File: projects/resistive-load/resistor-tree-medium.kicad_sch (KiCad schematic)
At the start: 24 parts, among them Q19 PJP45N06A_T0_00001, Q20 PJP45N06A_T0_00001, Q21 PJP45N06A_T0_00001, Q22 PJP45N06A_T0_00001

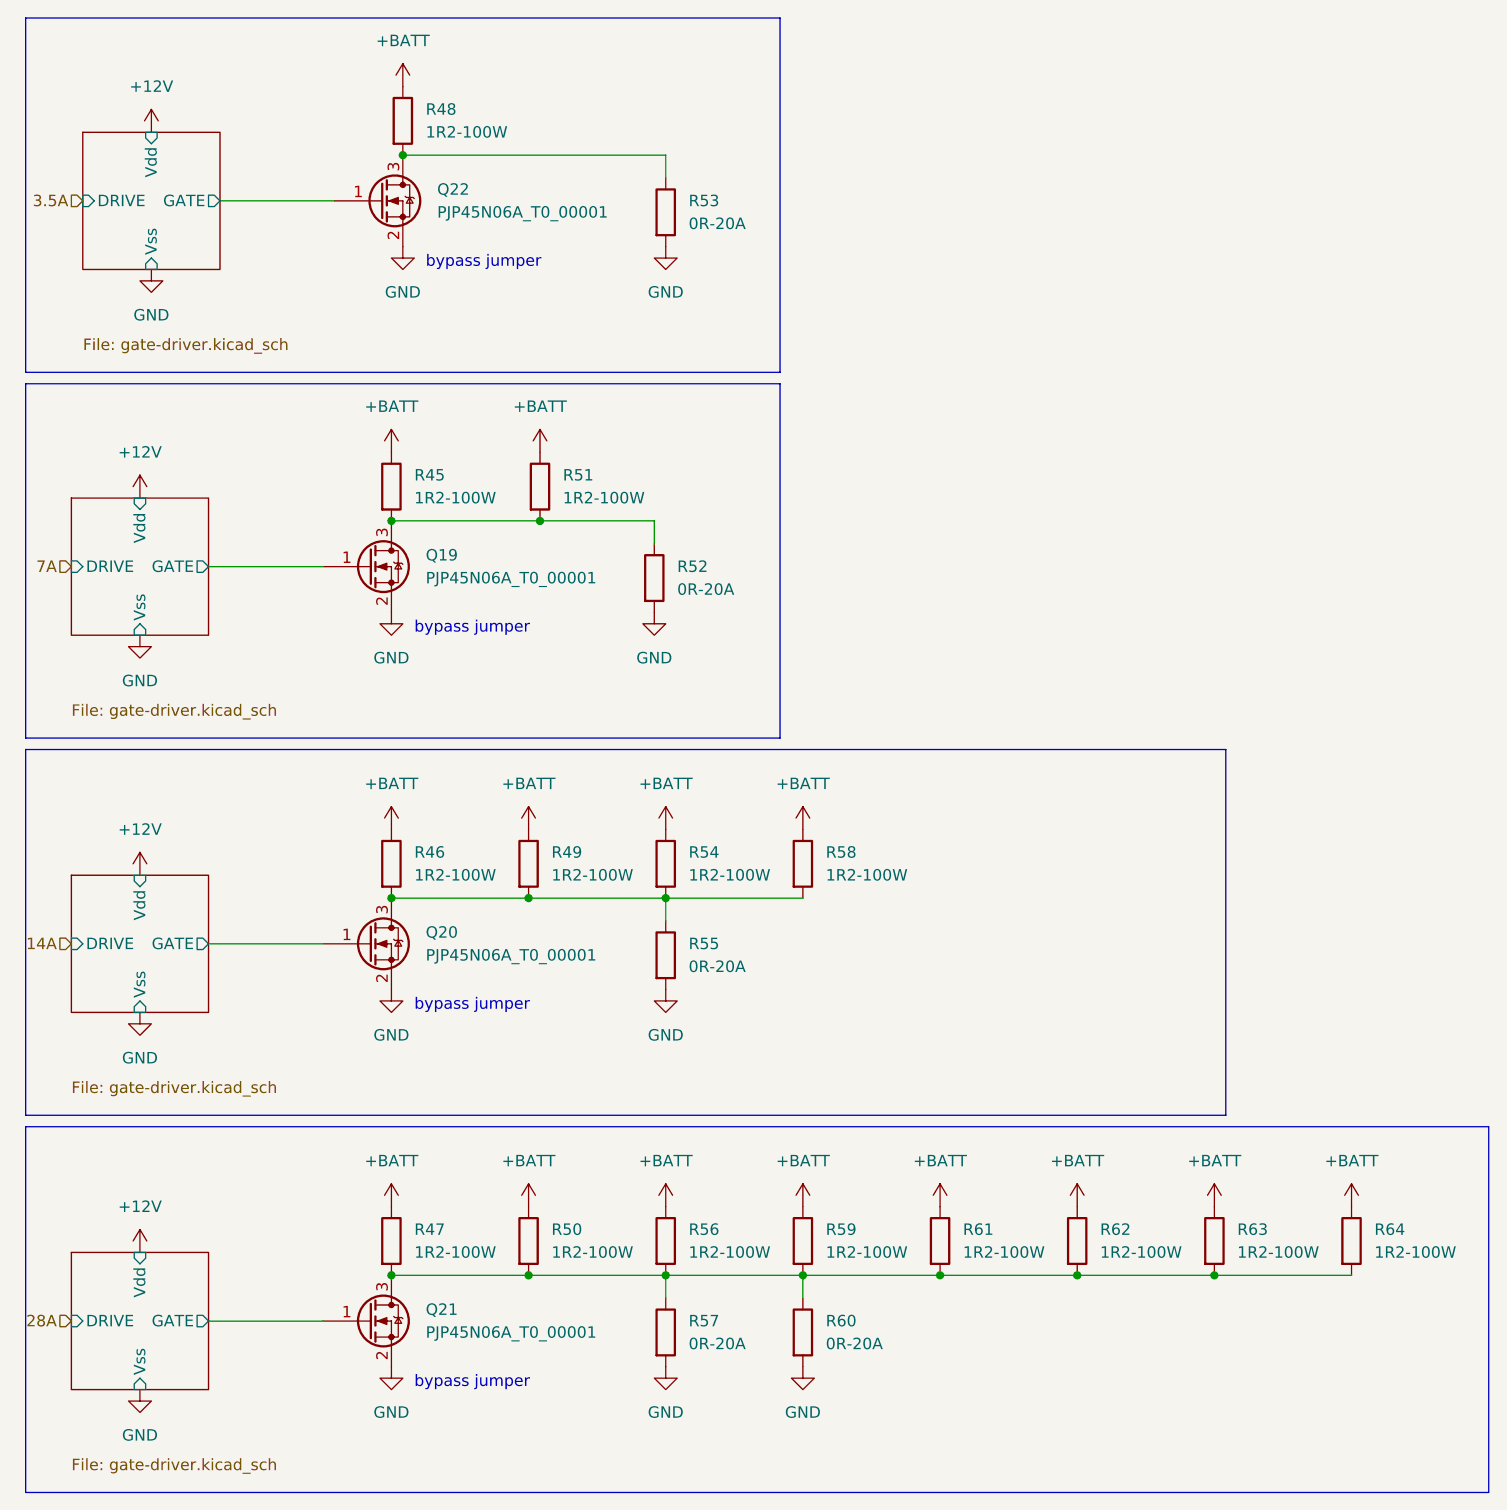
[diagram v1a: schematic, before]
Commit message: fix: update pin assignment for transistors
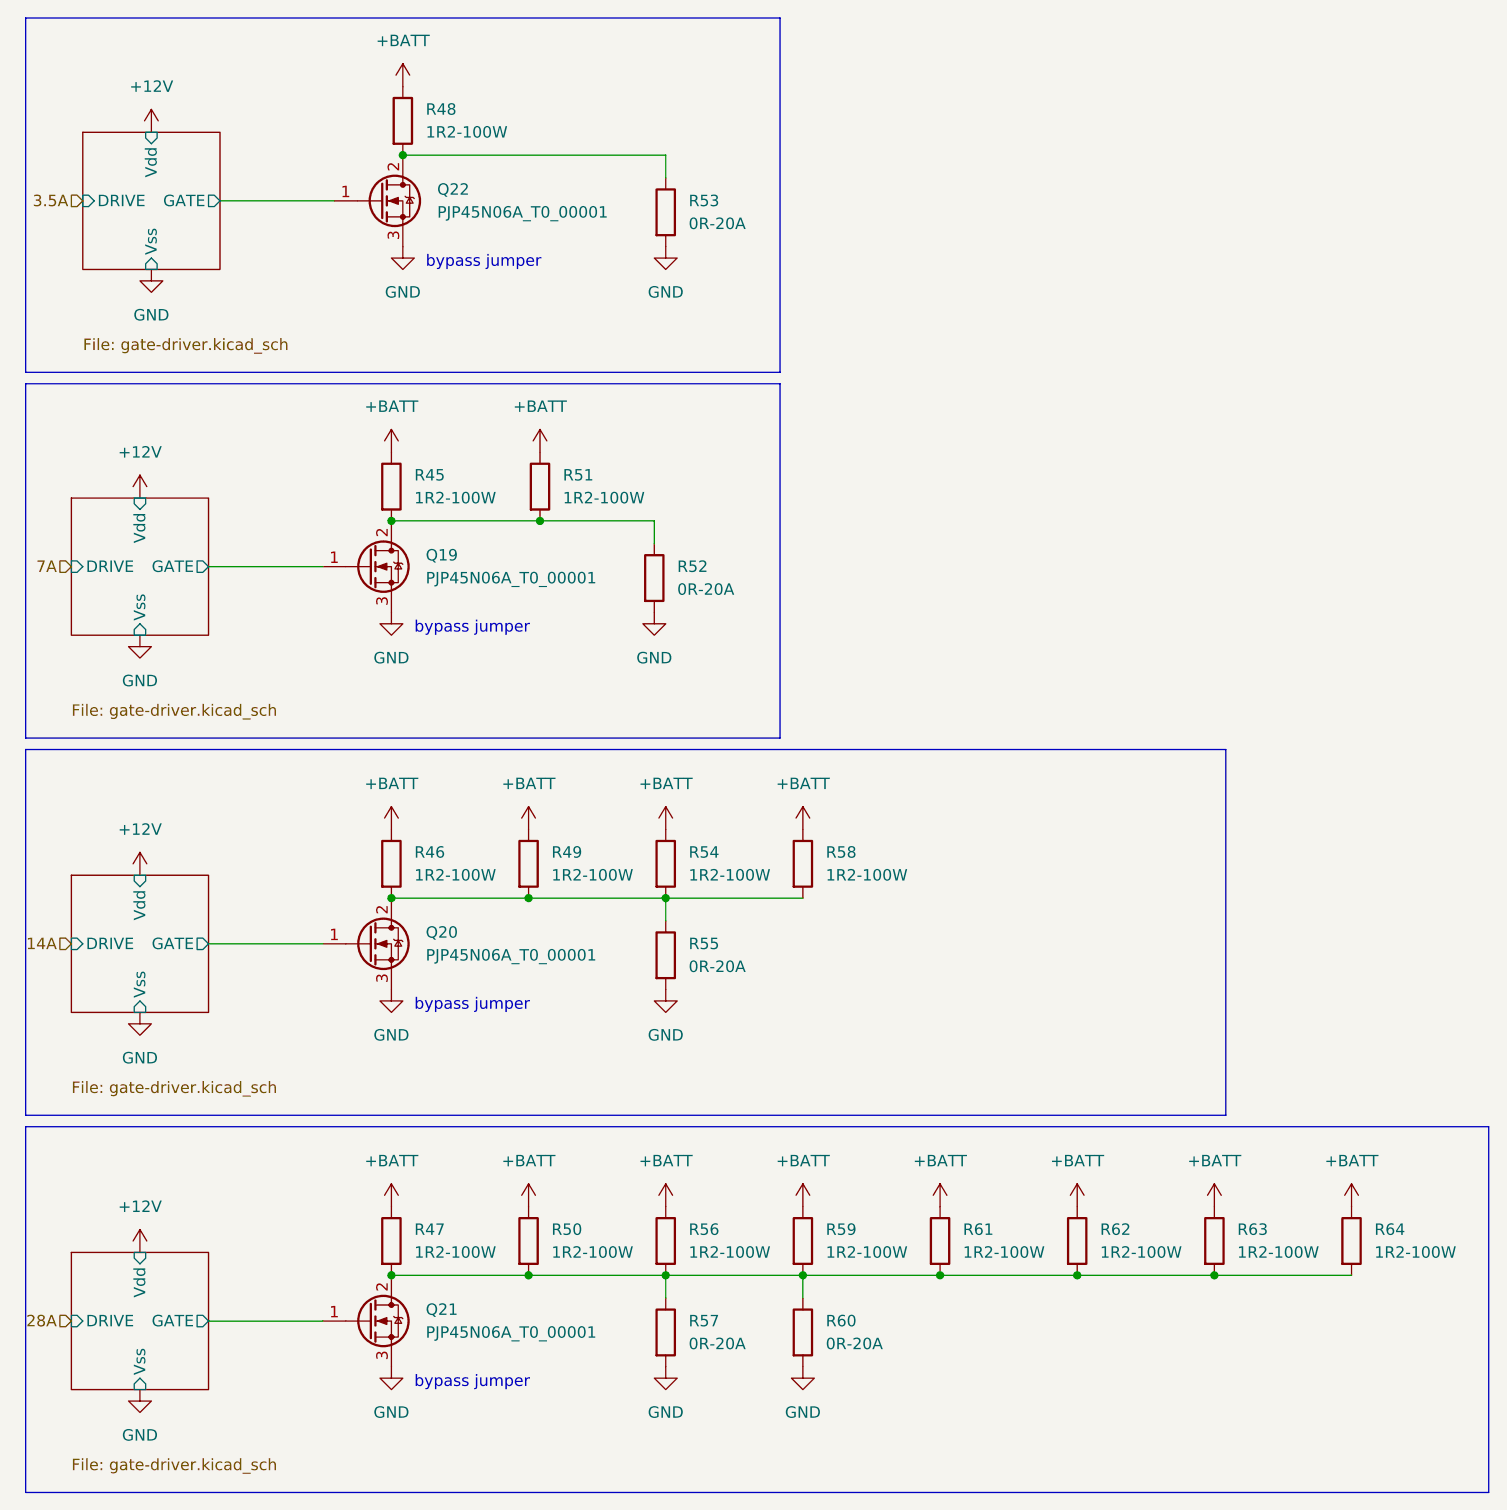
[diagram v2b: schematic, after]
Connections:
- net GND: now also Q19.3 (S), Q20.3 (S), Q21.3 (S), Q22.3 (S); no longer Q19.2 (S), Q20.2 (S), Q21.2 (S), Q22.2 (S)
- net at R47.2, R50.2, R56.2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: now also Q21.2 (D); no longer Q21.3 (D)
- net at R46.2, R49.2, R54.2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: now also Q20.2 (D); no longer Q20.3 (D)
- net at R48.2, R53.1: now also Q22.2 (D); no longer Q22.3 (D)
- net at R45.2, R51.2, R52.1: now also Q19.2 (D); no longer Q19.3 (D)
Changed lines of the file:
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@@
   (symbol (lib_id "power:GND") (at 82.55 80.01 0) (unit 1)
     (in_bom yes) (on_board yes) (fields_autoplaced)
-    (property "Reference" "#PWR0207" (id 0) (at 82.55 86.36 0)
+    (property "Reference" "#PWR?" (id 0) (at 82.55 86.36 0)
       (effects (font (size 1.27 1.27)) hide)
     )
@@
   (symbol (lib_id "power:+BATT") (at 68.58 104.14 0) (unit 1)
     (in_bom yes) (on_board yes) (fields_autoplaced)
-    (property "Reference" "#PWR0218" (id 0) (at 68.58 107.95 0)
+    (property "Reference" "#PWR?" (id 0) (at 68.58 107.95 0)
       (effects (font (size 1.27 1.27)) hide)
     )
@@
   (symbol (lib_id "power:GND") (at 25.4 82.55 0) (unit 1)
     (in_bom yes) (on_board yes) (fields_autoplaced)
-    (property "Reference" "#PWR0199" (id 0) (at 25.4 88.9 0)
+    (property "Reference" "#PWR?" (id 0) (at 25.4 88.9 0)
       (effects (font (size 1.27 1.27)) hide)
     )
@@
   (symbol (lib_id "power:+BATT") (at 53.34 146.05 0) (unit 1)
     (in_bom yes) (on_board yes) (fields_autoplaced)
-    (property "Reference" "#PWR0216" (id 0) (at 53.34 149.86 0)
+    (property "Reference" "#PWR?" (id 0) (at 53.34 149.86 0)
       (effects (font (size 1.27 1.27)) hide)
     )
@@
   (symbol (lib_id "power:+12V") (at 25.4 109.22 0) (unit 1)
     (in_bom yes) (on_board yes) (fields_autoplaced)
-    (property "Reference" "#PWR0214" (id 0) (at 25.4 113.03 0)
+    (property "Reference" "#PWR?" (id 0) (at 25.4 113.03 0)
       (effects (font (size 1.27 1.27)) hide)
     )
@@
   (symbol (lib_id "power:+BATT") (at 54.61 21.59 0) (unit 1)
     (in_bom yes) (on_board yes) (fields_autoplaced)
-    (property "Reference" "#PWR0201" (id 0) (at 54.61 25.4 0)
+    (property "Reference" "#PWR?" (id 0) (at 54.61 25.4 0)
       (effects (font (size 1.27 1.27)) hide)
     )
@@
   (symbol (lib_id "power:GND") (at 53.34 121.92 0) (unit 1)
     (in_bom yes) (on_board yes) (fields_autoplaced)
-    (property "Reference" "#PWR0212" (id 0) (at 53.34 128.27 0)
+    (property "Reference" "#PWR?" (id 0) (at 53.34 128.27 0)
       (effects (font (size 1.27 1.27)) hide)
     )
@@
   (symbol (lib_id "power:+12V") (at 25.4 151.13 0) (unit 1)
     (in_bom yes) (on_board yes) (fields_autoplaced)
-    (property "Reference" "#PWR0217" (id 0) (at 25.4 154.94 0)
+    (property "Reference" "#PWR?" (id 0) (at 25.4 154.94 0)
       (effects (font (size 1.27 1.27)) hide)
     )
@@
   (symbol (lib_id "power:GND") (at 83.82 163.83 0) (unit 1)
     (in_bom yes) (on_board yes) (fields_autoplaced)
-    (property "Reference" "#PWR0210" (id 0) (at 83.82 170.18 0)
+    (property "Reference" "#PWR?" (id 0) (at 83.82 170.18 0)
       (effects (font (size 1.27 1.27)) hide)
     )
@@
   (symbol (lib_id "power:+BATT") (at 114.3 146.05 0) (unit 1)
     (in_bom yes) (on_board yes) (fields_autoplaced)
-    (property "Reference" "#PWR0226" (id 0) (at 114.3 149.86 0)
+    (property "Reference" "#PWR?" (id 0) (at 114.3 149.86 0)
       (effects (font (size 1.27 1.27)) hide)
     )
@@
   (symbol (lib_id "power:+12V") (at 26.67 26.67 0) (unit 1)
     (in_bom yes) (on_board yes) (fields_autoplaced)
-    (property "Reference" "#PWR0200" (id 0) (at 26.67 30.48 0)
+    (property "Reference" "#PWR?" (id 0) (at 26.67 30.48 0)
       (effects (font (size 1.27 1.27)) hide)
     )
@@
   (symbol (lib_id "power:+BATT") (at 68.58 146.05 0) (unit 1)
     (in_bom yes) (on_board yes) (fields_autoplaced)
-    (property "Reference" "#PWR0219" (id 0) (at 68.58 149.86 0)
+    (property "Reference" "#PWR?" (id 0) (at 68.58 149.86 0)
       (effects (font (size 1.27 1.27)) hide)
     )
@@
   (symbol (lib_id "power:GND") (at 26.67 41.91 0) (unit 1)
     (in_bom yes) (on_board yes) (fields_autoplaced)
-    (property "Reference" "#PWR0202" (id 0) (at 26.67 48.26 0)
+    (property "Reference" "#PWR?" (id 0) (at 26.67 48.26 0)
       (effects (font (size 1.27 1.27)) hide)
     )
@@
   (symbol (lib_id "power:GND") (at 99.06 163.83 0) (unit 1)
     (in_bom yes) (on_board yes) (fields_autoplaced)
-    (property "Reference" "#PWR0223" (id 0) (at 99.06 170.18 0)
+    (property "Reference" "#PWR?" (id 0) (at 99.06 170.18 0)
       (effects (font (size 1.27 1.27)) hide)
     )
@@
   (symbol (lib_id "power:+BATT") (at 144.78 146.05 0) (unit 1)
     (in_bom yes) (on_board yes) (fields_autoplaced)
-    (property "Reference" "#PWR0229" (id 0) (at 144.78 149.86 0)
+    (property "Reference" "#PWR?" (id 0) (at 144.78 149.86 0)
       (effects (font (size 1.27 1.27)) hide)
     )
@@
   (symbol (lib_id "power:+BATT") (at 83.82 146.05 0) (unit 1)
     (in_bom yes) (on_board yes) (fields_autoplaced)
-    (property "Reference" "#PWR0220" (id 0) (at 83.82 149.86 0)
+    (property "Reference" "#PWR?" (id 0) (at 83.82 149.86 0)
       (effects (font (size 1.27 1.27)) hide)
     )
@@
   (symbol (lib_id "power:+BATT") (at 83.82 104.14 0) (unit 1)
     (in_bom yes) (on_board yes) (fields_autoplaced)
-    (property "Reference" "#PWR0221" (id 0) (at 83.82 107.95 0)
+    (property "Reference" "#PWR?" (id 0) (at 83.82 107.95 0)
       (effects (font (size 1.27 1.27)) hide)
     )
@@
   (symbol (lib_id "power:+12V") (at 25.4 67.31 0) (unit 1)
     (in_bom yes) (on_board yes) (fields_autoplaced)
-    (property "Reference" "#PWR0198" (id 0) (at 25.4 71.12 0)
+    (property "Reference" "#PWR?" (id 0) (at 25.4 71.12 0)
       (effects (font (size 1.27 1.27)) hide)
     )
@@
   (symbol (lib_id "power:+BATT") (at 53.34 62.23 0) (unit 1)
     (in_bom yes) (on_board yes) (fields_autoplaced)
-    (property "Reference" "#PWR0205" (id 0) (at 53.34 66.04 0)
+    (property "Reference" "#PWR?" (id 0) (at 53.34 66.04 0)
       (effects (font (size 1.27 1.27)) hide)
     )
@@
   (symbol (lib_id "power:GND") (at 25.4 166.37 0) (unit 1)
     (in_bom yes) (on_board yes) (fields_autoplaced)
-    (property "Reference" "#PWR0209" (id 0) (at 25.4 172.72 0)
+    (property "Reference" "#PWR?" (id 0) (at 25.4 172.72 0)
       (effects (font (size 1.27 1.27)) hide)
     )
@@
   (symbol (lib_id "power:+BATT") (at 99.06 146.05 0) (unit 1)
     (in_bom yes) (on_board yes) (fields_autoplaced)
-    (property "Reference" "#PWR0225" (id 0) (at 99.06 149.86 0)
+    (property "Reference" "#PWR?" (id 0) (at 99.06 149.86 0)
       (effects (font (size 1.27 1.27)) hide)
     )
@@
   (symbol (lib_id "power:+BATT") (at 160.02 146.05 0) (unit 1)
     (in_bom yes) (on_board yes) (fields_autoplaced)
-    (property "Reference" "#PWR0228" (id 0) (at 160.02 149.86 0)
+    (property "Reference" "#PWR?" (id 0) (at 160.02 149.86 0)
       (effects (font (size 1.27 1.27)) hide)
     )
@@
   (symbol (lib_id "power:+BATT") (at 99.06 104.14 0) (unit 1)
     (in_bom yes) (on_board yes) (fields_autoplaced)
-    (property "Reference" "#PWR0224" (id 0) (at 99.06 107.95 0)
+    (property "Reference" "#PWR?" (id 0) (at 99.06 107.95 0)
       (effects (font (size 1.27 1.27)) hide)
     )
@@
   (symbol (lib_id "power:GND") (at 53.34 163.83 0) (unit 1)
     (in_bom yes) (on_board yes) (fields_autoplaced)
-    (property "Reference" "#PWR0211" (id 0) (at 53.34 170.18 0)
+    (property "Reference" "#PWR?" (id 0) (at 53.34 170.18 0)
       (effects (font (size 1.27 1.27)) hide)
     )
@@
   (symbol (lib_id "power:GND") (at 54.61 39.37 0) (unit 1)
     (in_bom yes) (on_board yes) (fields_autoplaced)
-    (property "Reference" "#PWR0203" (id 0) (at 54.61 45.72 0)
+    (property "Reference" "#PWR?" (id 0) (at 54.61 45.72 0)
       (effects (font (size 1.27 1.27)) hide)
     )
@@
   (symbol (lib_id "power:GND") (at 53.34 80.01 0) (unit 1)
     (in_bom yes) (on_board yes) (fields_autoplaced)
-    (property "Reference" "#PWR0208" (id 0) (at 53.34 86.36 0)
+    (property "Reference" "#PWR?" (id 0) (at 53.34 86.36 0)
       (effects (font (size 1.27 1.27)) hide)
     )
@@
   (symbol (lib_id "power:+BATT") (at 129.54 146.05 0) (unit 1)
     (in_bom yes) (on_board yes) (fields_autoplaced)
-    (property "Reference" "#PWR0227" (id 0) (at 129.54 149.86 0)
+    (property "Reference" "#PWR?" (id 0) (at 129.54 149.86 0)
       (effects (font (size 1.27 1.27)) hide)
     )
@@
   (symbol (lib_id "power:GND") (at 83.82 39.37 0) (unit 1)
     (in_bom yes) (on_board yes) (fields_autoplaced)
-    (property "Reference" "#PWR0204" (id 0) (at 83.82 45.72 0)
+    (property "Reference" "#PWR?" (id 0) (at 83.82 45.72 0)
       (effects (font (size 1.27 1.27)) hide)
     )
@@
   (symbol (lib_id "power:+BATT") (at 69.85 62.23 0) (unit 1)
     (in_bom yes) (on_board yes) (fields_autoplaced)
-    (property "Reference" "#PWR0206" (id 0) (at 69.85 66.04 0)
+    (property "Reference" "#PWR?" (id 0) (at 69.85 66.04 0)
       (effects (font (size 1.27 1.27)) hide)
     )
@@
   (symbol (lib_id "power:GND") (at 25.4 124.46 0) (unit 1)
     (in_bom yes) (on_board yes) (fields_autoplaced)
-    (property "Reference" "#PWR0213" (id 0) (at 25.4 130.81 0)
+    (property "Reference" "#PWR?" (id 0) (at 25.4 130.81 0)
       (effects (font (size 1.27 1.27)) hide)
     )
@@
     (pin "1")
   )
-  (symbol (lib_name "PJP45N06A_T0_00001_3") (lib_id "OEM:PJP45N06A_T0_00001") (at 50.8 116.84 0) (unit 1)
+  (symbol (lib_id "OEM:PJP45N06A_T0_00001") (at 50.8 116.84 0) (unit 1)
     (in_bom yes) (on_board yes)
     (property "Reference" "Q20" (id 0) (at 57.15 115.5699 0)
@@
   (symbol (lib_id "power:+BATT") (at 53.34 104.14 0) (unit 1)
     (in_bom yes) (on_board yes) (fields_autoplaced)
-    (property "Reference" "#PWR0215" (id 0) (at 53.34 107.95 0)
+    (property "Reference" "#PWR?" (id 0) (at 53.34 107.95 0)
       (effects (font (size 1.27 1.27)) hide)
     )
@@
   (symbol (lib_id "power:GND") (at 83.82 121.92 0) (unit 1)
     (in_bom yes) (on_board yes) (fields_autoplaced)
-    (property "Reference" "#PWR0222" (id 0) (at 83.82 128.27 0)
-      (effects (font (size 1.27 1.27)) hide)
-    )
+    (property "Reference" "#PWR?" (id 0) (at 83.82 128.27 0)
+      (effects (font (size 1.27 1.27)) hide)
+    )
